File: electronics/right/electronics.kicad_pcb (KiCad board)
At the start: 2 copper layers, 109.6 x 73.9 mm, 90 parts, among them J3 USB_C_Receptacle_USB2.0, J4 Battery Connector, SW23 Choc v1 Socket, SW24 Choc v1 Socket, SW25 Choc v1 Socket, SW26 Choc v1 Socket, SW27 Choc v1 Socket, SW28 Choc v1 Socket, SW29 Choc v1 Socket, SW30 Choc v1 Socket, SW31 Choc v1 Socket, SW32 Choc v1 Socket, SW33 Choc v1 Socket, SW34 Choc v1 Socket, SW35 Choc v1 Socket, SW36 Choc v1 Socket, SW37 Choc v1 Socket, SW38 Choc v1 Socket, SW39 Choc v1 Socket, SW40 Choc v1 Socket, SW41 Choc v1 Socket, SW42 Choc v1 Socket, SW43 Choc v1 Socket, SW44 SW_Reset, U4 nRF52840, U5 ESDR0502NMUTAG, U6 BQ24075RGT, Y3 32.768 kHz, Y4 32MHz

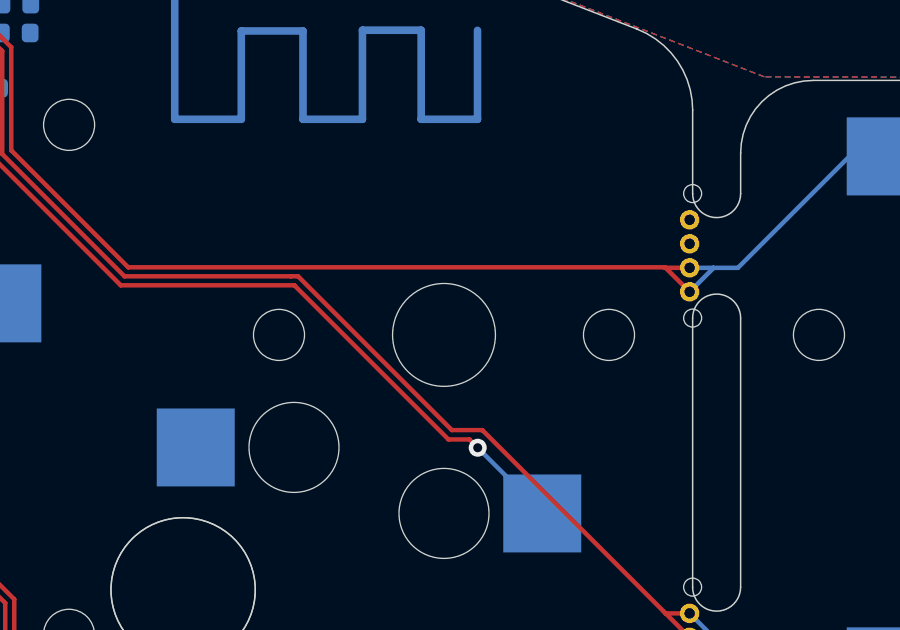
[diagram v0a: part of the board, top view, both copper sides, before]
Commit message: Extend ground plane fill.
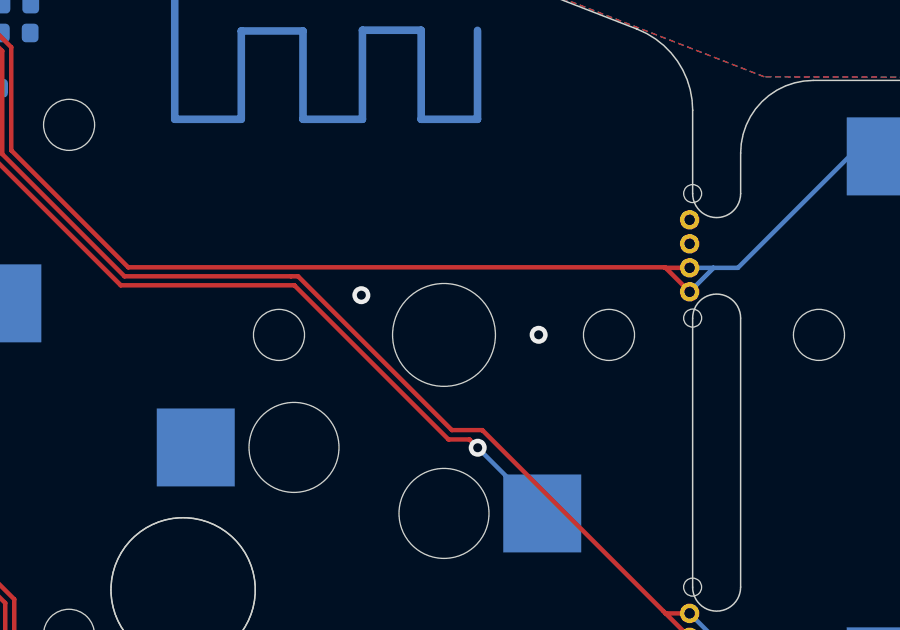
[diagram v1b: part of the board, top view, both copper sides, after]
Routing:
- net GND: vias 35 -> 37
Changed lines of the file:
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@@
   (via locked (at 82.38 33.089) (size 0.6) (drill 0.3) (layers "F.Cu" "B.Cu") (net 2))
   (via locked (at 86.94 29.25) (size 0.6) (drill 0.3) (layers "F.Cu" "B.Cu") (net 2))
+  (via (at 113.21 45.08) (size 0.6) (drill 0.3) (layers "F.Cu" "B.Cu") (free) (net 2))
   (via locked (at 104.84 32.239) (size 0.6) (drill 0.3) (layers "F.Cu" "B.Cu") (free) (net 2))
   (via locked (at 91.94 33.239) (size 0.6) (drill 0.3) (layers "F.Cu" "B.Cu") (free) (net 2))
@@
   (via locked (at 61.74 34.0995) (size 0.6) (drill 0.3) (layers "F.Cu" "B.Cu") (net 2))
   (via locked (at 81.58 33.089) (size 0.6) (drill 0.3) (layers "F.Cu" "B.Cu") (net 2))
+  (via (at 119.12 46.4) (size 0.6) (drill 0.3) (layers "F.Cu" "B.Cu") (free) (net 2))
   (via locked (at 95.54 30.839) (size 0.6) (drill 0.3) (layers "F.Cu" "B.Cu") (free) (net 2))
   (via locked (at 91.94 30.839) (size 0.6) (drill 0.3) (layers "F.Cu" "B.Cu") (free) (net 2))

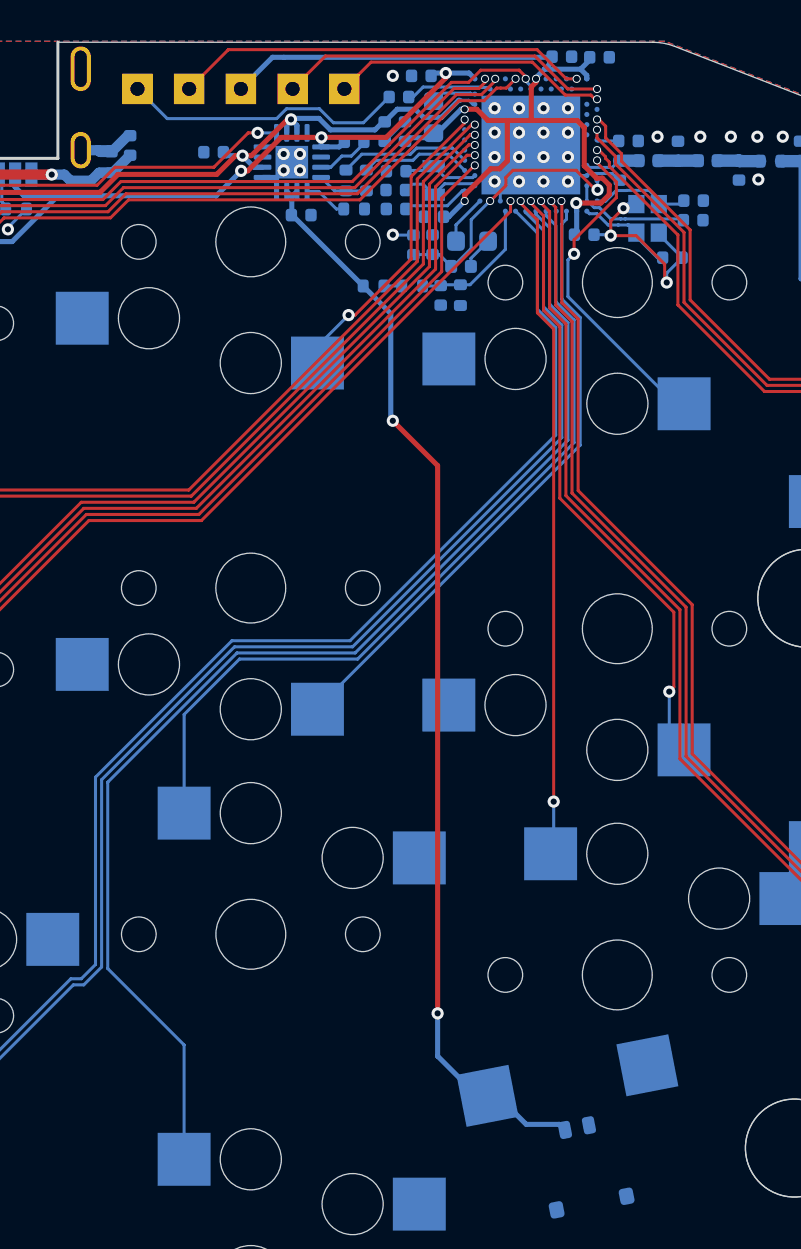
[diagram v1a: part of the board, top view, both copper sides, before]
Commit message: electronics/right: Fix schema and PCB references parity.
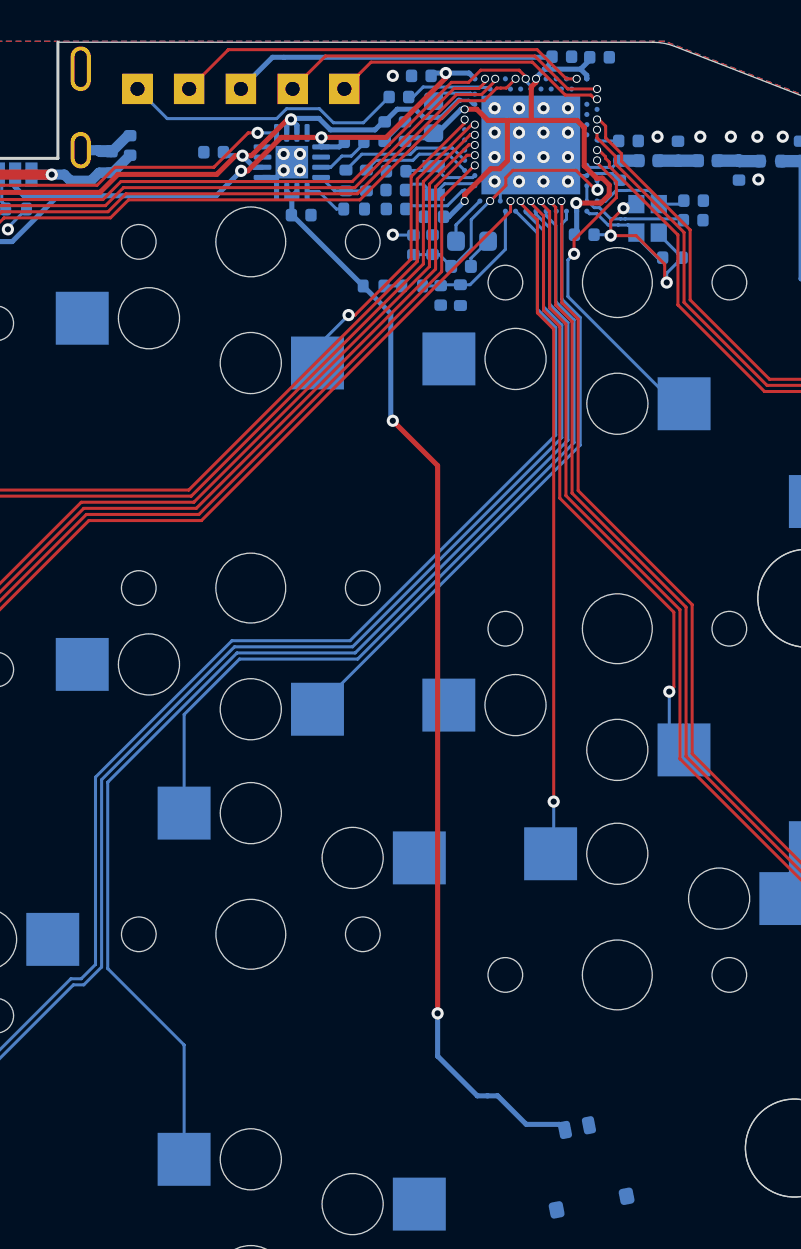
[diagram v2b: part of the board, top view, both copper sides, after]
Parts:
- removed ?: , 
- removed ?: , clipboard:cb50c767-9c7e-4e33-9f10-2a6feed7503c
- removed AE2: Antenna, lib:2.4GHz-meander-antenna-right
- removed C27, C31, C50: 1uF, lib:C_0402_1005Metric
- removed C28: 47nF, lib:C_0402_1005Metric
- removed C29, C30, C36, C37, C51, C52: 4.7uF, lib:C_0402_1005Metric
- removed C32, C33, C34, C40, C49: 100nF, lib:C_0402_1005Metric
- removed C35: 1nF, lib:C_0402_1005Metric
- removed C38: 100pF, lib:C_0402_1005Metric
- removed C39, C42, C47, C48: 15pF, lib:C_0402_1005Metric
- removed C41: 10nF, lib:C_0402_1005Metric
- removed C43: 1.5pF, lib:C_0402_1005Metric
- removed C44: N.C, lib:C_0402_1005Metric
- removed C45: 1.2pF, lib:C_0402_1005Metric
- removed C46: 1.0pF, lib:C_0402_1005Metric
- removed D3, D4: LED_Dual_KKA, lib:LED-ARRAY-SMD_3P-L3.0-W2.0-L-FD
- removed H5, H6, H7, H8: MountingHole, lib:screw-hole
- removed J3: USB_C_Receptacle_USB2.0, lib:USB-C-SMD_TYPE-C-31-M-13A-1
- removed J4: Battery Connector, lib:Molex_Pico-EZmate_78171-0002_1x02-1MP_P1.20mm_Vertical
- removed L10: 4.7nH, Inductor_SMD:L_0402_1005Metric
- removed L6: 15nH, Inductor_SMD:L_0402_1005Metric
- removed L7, L8: 10uH, Inductor_SMD:L_0603_1608Metric
- removed L9: 2.2nH, Inductor_SMD:L_0402_1005Metric
- removed NT2: NetTie_2, lib:net-tie-2-tiny
- removed R13: 10M, lib:R_0402_1005Metric
- removed R14, R15: 2M, lib:R_0402_1005Metric
- removed R16: 0R, lib:R_0402_1005Metric
- removed R17: 1.5k, lib:R_0402_1005Metric
- removed R18: 1M, lib:R_0402_1005Metric
- removed R19, R20: 5.1k, lib:R_0402_1005Metric
- removed R21, R22, R23: 10k, lib:R_0402_1005Metric
- removed R24: 3.9k, lib:R_0402_1005Metric
- removed SW23, SW24, SW25, SW26, SW27, SW28, SW29, SW30, SW31, SW32, SW33, SW34, SW35, SW36, SW37, SW38, SW39, SW40, SW41, SW42, SW43: Choc v1 Socket, lib:Kailh_socket_PG1350
- removed SW44: SW_Reset, lib:Panasonic_EVQPUL_EVQPUC
- removed TP10: GND, TestPoint:TestPoint_THTPad_1.5x1.5mm_Drill0.7mm
- removed TP6: SWO, TestPoint:TestPoint_THTPad_1.5x1.5mm_Drill0.7mm
- removed TP7: SWC, TestPoint:TestPoint_THTPad_1.5x1.5mm_Drill0.7mm
- removed TP8: SWD, TestPoint:TestPoint_THTPad_1.5x1.5mm_Drill0.7mm
- removed TP9: 3.3V, TestPoint:TestPoint_THTPad_1.5x1.5mm_Drill0.7mm
- removed U4: nRF52840, Package_DFN_QFN:Nordic_AQFN-73-1EP_7x7mm_P0.5mm
- removed U5: ESDR0502NMUTAG, lib:ESDR0502NMUTAG
- removed U6: BQ24075RGT, lib:VQFN-16-1EP_3x3mm_P0.5mm_EP1.6x1.6mm
- removed Y3: 32.768 kHz, lib:Crystal_SMD_2012-2Pin_2.0x1.2mm
- removed Y4: 32MHz, lib:Crystal_SMD_2016-4Pin_2.0x1.6mm
- added AE1: Antenna, lib:2.4GHz-meander-antenna-right, F.Cu at (107.0, 33.5)
- added C1: 1uF, Capacitor_SMD:C_0402_1005Metric, B.Cu at (88.9, 37.5)
- added C10: 4.7uF, Capacitor_SMD:C_0402_1005Metric, B.Cu at (88.3, 29.3)
- added C11: 4.7uF, Capacitor_SMD:C_0402_1005Metric, B.Cu at (87.2, 30.3)
- added C12: 100pF, Capacitor_SMD:C_0402_1005Metric, B.Cu at (101.7, 36.3)
- added C13: 15pF, Capacitor_SMD:C_0402_1005Metric, B.Cu at (87.1, 34.9)
- added C14: 100nF, Capacitor_SMD:C_0402_1005Metric, B.Cu at (87.1, 35.8)
- added C15: 10nF, Capacitor_SMD:C_0402_1005Metric, B.Cu at (89.3, 40.0)
- added C16: 15pF, Capacitor_SMD:C_0402_1005Metric, B.Cu at (87.1, 33.9)
- added C17: 1.5pF, Capacitor_SMD:C_0402_1005Metric, B.Cu at (106.9, 32.9)
- added C18: N.C, Capacitor_SMD:C_0402_1005Metric, B.Cu at (103.9, 33.9)
- added C19: 1.2pF, Capacitor_SMD:C_0402_1005Metric, B.Cu at (100.9, 32.9)
- added C2: 47nF, Capacitor_SMD:C_0402_1005Metric, B.Cu at (88.0, 37.5)
- added C20: 1.0pF, Capacitor_SMD:C_0402_1005Metric, B.Cu at (98.1, 33.9)
- added C21: 15pF, Capacitor_SMD:C_0402_1005Metric, B.Cu at (101.7, 35.4)
- added C22: 15pF, Capacitor_SMD:C_0402_1005Metric, B.Cu at (100.7, 38.2)
- added C23: 100nF, Capacitor_SMD:C_0402_1005Metric, B.Cu at (74.0, 32.7)
- added C24: 1uF, Capacitor_SMD:C_0402_1005Metric, B.Cu at (85.0, 32.5)
- added C25: 4.7uF, Capacitor_SMD:C_0402_1005Metric, B.Cu at (86.5, 32.0)
- added C26: 4.7uF, Capacitor_SMD:C_0402_1005Metric, B.Cu at (82.4, 36.1)
- added C3: 4.7uF, Capacitor_SMD:C_0402_1005Metric, B.Cu at (78.1, 33.0)
- added C4: 4.7uF, Capacitor_SMD:C_0402_1005Metric, B.Cu at (87.5, 32.0)
- added C5: 1uF, Capacitor_SMD:C_0402_1005Metric, B.Cu at (96.3, 37.0)
- added C6: 100nF, Capacitor_SMD:C_0402_1005Metric, B.Cu at (95.2, 28.3)
- added C7: 100nF, Capacitor_SMD:C_0402_1005Metric, B.Cu at (97.1, 28.3)
- added C8: 100nF, Capacitor_SMD:C_0402_1005Metric, B.Cu at (89.0, 36.2)
- added C9: 1nF, Capacitor_SMD:C_0402_1005Metric, B.Cu at (98.5, 32.4)
- added D1: LED_Dual_KKA, lib:LED-ARRAY-SMD_3P-L3.0-W2.0-L-FD, B.Cu at (41.8, 34.3)
- added D2: LED_Dual_KKA, lib:LED-ARRAY-SMD_3P-L3.0-W2.0-L-FD, B.Cu at (54.3, 30.5)
- added H1: MountingHole, lib:screw-hole, F.Cu at (52.7, 52.9)
- added H2: MountingHole, lib:screw-hole, F.Cu at (107.3, 54.9)
- added H3: MountingHole, lib:screw-hole, F.Cu at (53.3, 83.9)
- added H4: MountingHole, lib:screw-hole, B.Cu at (106.7, 81.9)
- added J1: USB_C_Receptacle_USB2.0, lib:USB-C-SMD_TYPE-C-31-M-13A-1, B.Cu at (66.0, 31.5)
- added J2: Molex_781710002, lib:Molex_Pico-EZmate_78171-0002_1x02-1MP_P1.20mm_Vertical, B.Cu at (96.3, 82.7)
- added L1: 15nH, Inductor_SMD:L_0402_1005Metric, B.Cu at (90.3, 38.6)
- added L2: 10uH, Inductor_SMD:L_0603_1608Metric, B.Cu at (90.8, 37.4)
- added L3: 10uH, Inductor_SMD:L_0603_1608Metric, B.Cu at (88.9, 31.3)
- added L4: 2.2nH, Inductor_SMD:L_0402_1005Metric, B.Cu at (102.4, 33.4)
- added L5: 4.7nH, Inductor_SMD:L_0402_1005Metric, B.Cu at (99.5, 33.4)
- added NT1: NetTie_2, lib:net-tie-2-tiny, B.Cu at (96.2, 34.1)
- added R1: 10M, Resistor_SMD:R_0402_1005Metric, B.Cu at (90.3, 40.0)
- added R10: 10k, Resistor_SMD:R_0402_1005Metric, B.Cu at (85.6, 34.4)
- added R11: 10k, Resistor_SMD:R_0402_1005Metric, B.Cu at (53.3, 33.2)
- added R12: 3.9k, Resistor_SMD:R_0402_1005Metric, B.Cu at (84.6, 34.4)
- added R2: 2M, Resistor_SMD:R_0402_1005Metric, B.Cu at (87.9, 39.6)
- added R3: 2M, Resistor_SMD:R_0402_1005Metric, B.Cu at (86.0, 39.6)
- added R4: 0R, Resistor_SMD:R_0402_1005Metric, B.Cu at (105.5, 33.4)
- added R5: 1.5k, Resistor_SMD:R_0402_1005Metric, B.Cu at (41.2, 36.3)
- added R6: 1M, Resistor_SMD:R_0402_1005Metric, B.Cu at (73.1, 33.5)
- added R7: 5.1k, Resistor_SMD:R_0402_1005Metric, B.Cu at (68.4, 35.8)
- added R8: 5.1k, Resistor_SMD:R_0402_1005Metric, B.Cu at (64.2, 36.0)
- added R9: 10k, Resistor_SMD:R_0402_1005Metric, B.Cu at (85.0, 35.8)
- added SW1: CPG135001S30, lib:Kailh_socket_PG1350, B.Cu at (44.0, 44.4)
- added SW10: CPG135001S30, lib:Kailh_socket_PG1350, B.Cu at (98.0, 56.4)
- added SW11: CPG135001S30, lib:Kailh_socket_PG1350, B.Cu at (116.0, 63.4)
- added SW12: CPG135001S30, lib:Kailh_socket_PG1350, B.Cu at (134.0, 63.4)
- added SW13: CPG135001S30, lib:Kailh_socket_PG1350, B.Cu at (44.0, 78.4)
- added SW14: CPG135001S30, lib:Kailh_socket_PG1350, B.Cu at (62.0, 75.4)
- added SW15: CPG135001S30, lib:Kailh_socket_PG1350, B.Cu at (80.0, 71.4)
- added SW16: CPG135001S30, lib:Kailh_socket_PG1350, B.Cu at (98.0, 73.4)
- added SW17: CPG135001S30, lib:Kailh_socket_PG1350, B.Cu at (116.0, 80.4)
- added SW18: CPG135001S30, lib:Kailh_socket_PG1350, B.Cu at (134.0, 80.4)
- added SW19: CPG135001S30, lib:Kailh_socket_PG1350, B.Cu at (44.0, 95.4)
- added SW2: CPG135001S30, lib:Kailh_socket_PG1350, B.Cu at (62.0, 41.4)
- added SW20: CPG135001S30, lib:Kailh_socket_PG1350, B.Cu at (62.0, 92.4)
- added SW21: CPG135001S30, lib:Kailh_socket_PG1350, B.Cu at (80.0, 88.4)
- added SW22: EVQPUC02K, lib:Panasonic_EVQPUL_EVQPUC, B.Cu at (48.3, 33.2)
- added SW3: CPG135001S30, lib:Kailh_socket_PG1350, B.Cu at (80.0, 37.4)
- added SW4: CPG135001S30, lib:Kailh_socket_PG1350, B.Cu at (98.0, 39.4)
- added SW5: CPG135001S30, lib:Kailh_socket_PG1350, B.Cu at (116.0, 46.4)
- added SW6: CPG135001S30, lib:Kailh_socket_PG1350, B.Cu at (134.0, 46.4)
- added SW7: CPG135001S30, lib:Kailh_socket_PG1350, B.Cu at (44.0, 61.4)
- added SW8: CPG135001S30, lib:Kailh_socket_PG1350, B.Cu at (62.0, 58.4)
- added SW9: CPG135001S30, lib:Kailh_socket_PG1350, B.Cu at (80.0, 54.4)
- added TP1: SWO, TestPoint:TestPoint_THTPad_1.5x1.5mm_Drill0.7mm, B.Cu at (76.9, 29.9)
- added TP2: SWC, TestPoint:TestPoint_THTPad_1.5x1.5mm_Drill0.7mm, B.Cu at (84.6, 29.9)
- added TP3: SWD, TestPoint:TestPoint_THTPad_1.5x1.5mm_Drill0.7mm, B.Cu at (82.0, 29.9)
- added TP4: 3.3V, TestPoint:TestPoint_THTPad_1.5x1.5mm_Drill0.7mm, B.Cu at (79.5, 29.9)
- added TP5: GND, TestPoint:TestPoint_THTPad_1.5x1.5mm_Drill0.7mm, B.Cu at (74.4, 29.9)
- added U1: nRF52840, Package_DFN_QFN:Nordic_AQFN-73-1EP_7x7mm_P0.5mm, B.Cu at (93.7, 32.6)
- added U2: ESDR0502NMUTAG, lib:ESDR0502NMUTAG, B.Cu at (65.5, 37.0)
- added U3: BQ24075RGT, Package_DFN_QFN:VQFN-16-1EP_3x3mm_P0.5mm_EP1.6x1.6mm, B.Cu at (82.0, 33.5)
- added Y1: 32.768 kHz, lib:Crystal_SMD_2012-2Pin_2.0x1.2mm, B.Cu at (88.9, 34.4)
- added Y2: 32MHz, lib:Crystal_SMD_2016-4Pin_2.0x1.6mm, B.Cu at (99.5, 36.2)
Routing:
- net Net-(U4-P0.15): track 55.2 -> 0.00 mm, vias 2 -> 0
- net Net-(U1-P0.15): track 0.00 -> 55.2 mm, vias 0 -> 2
- net Net-(U4-D+): track 35.0 -> 0.00 mm, vias 3 -> 0
- net Net-(U1-D+): track 0.00 -> 35.0 mm, vias 0 -> 3
- net Net-(U4-D-): track 32.7 -> 0.00 mm, vias 3 -> 0
- net Net-(U1-D-): track 0.00 -> 32.7 mm, vias 0 -> 3
- net Net-(D4-K2): track 29.5 -> 0.00 mm, vias 2 -> 0
- net Net-(D2-K2): track 0.00 -> 29.5 mm, vias 0 -> 2
- net Net-(U4-TRACEDATA0/P1.00): track 20.3 -> 0.00 mm, vias 1 -> 0
- net Net-(U1-TRACEDATA0/P1.00): track 0.00 -> 20.3 mm, vias 0 -> 1
- net Net-(U4-SWDIO): track 16.1 -> 0.00 mm, vias 1 -> 0
- net Net-(U1-SWDIO): track 0.00 -> 16.1 mm, vias 0 -> 1
- net Net-(U4-SWDCLK): track 13.7 -> 0.00 mm, vias 1 -> 0
- net Net-(U1-SWDCLK): track 0.00 -> 13.7 mm, vias 0 -> 1
- net Net-(U4-DEC4): track 13.0 -> 0.00 mm, vias 2 -> 0
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
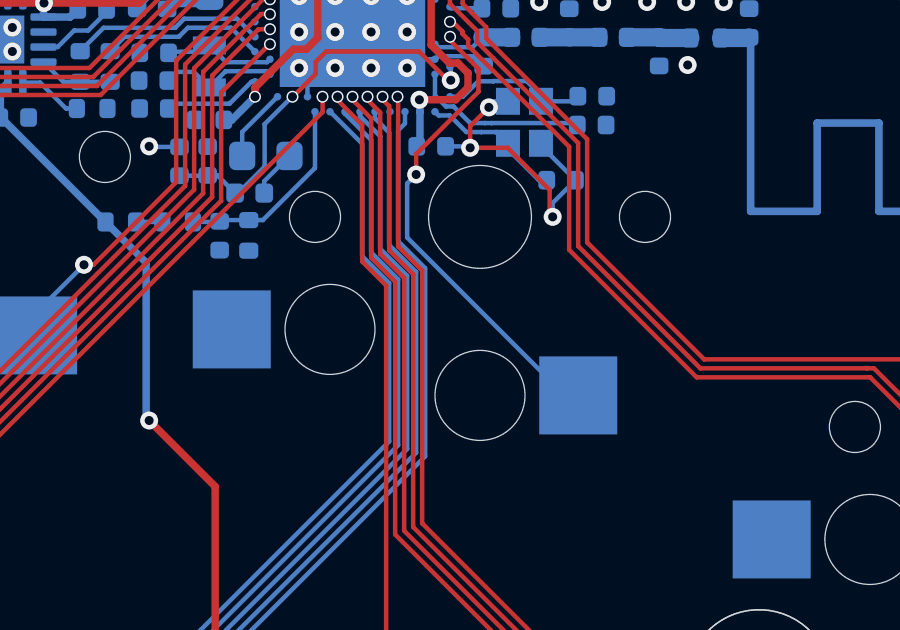
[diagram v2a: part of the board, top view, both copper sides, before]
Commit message: Remove footprint placement silkscreen lines.
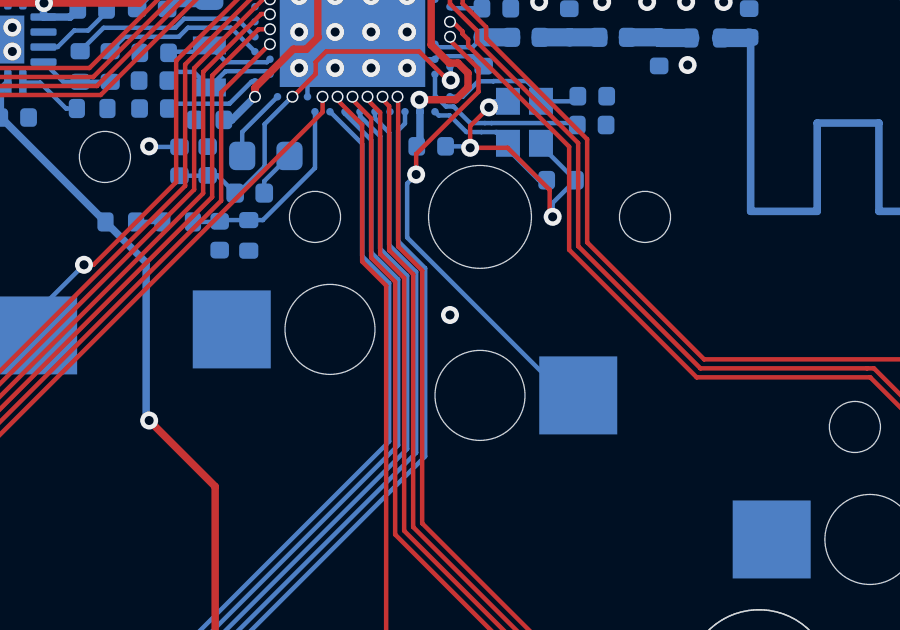
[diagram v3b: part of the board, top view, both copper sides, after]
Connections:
- mouse-bite-5mm-slot pad : K6 -> GND
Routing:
- net GND: vias 37 -> 38
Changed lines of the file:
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@@
     (pad "" thru_hole circle locked (at 1.675 -0.1 90) (size 0.65 0.65) (drill 0.35) (layers "*.Cu" "*.Mask")
       (net 15 "K6"))
-    (pad "" thru_hole circle locked (at 2.475 -0.1 90) (size 0.65 0.65) (drill 0.35) (layers "*.Cu" "*.Mask"))
-    (pad "" thru_hole circle locked (at 3.275 -0.1 90) (size 0.65 0.65) (drill 0.35) (layers "*.Cu" "*.Mask"))
+    (pad "" thru_hole circle locked (at 2.475 -0.1 90) (size 0.65 0.65) (drill 0.35) (layers "*.Cu" "*.Mask")
+      (net 2 "GND"))
+    (pad "" thru_hole circle locked (at 3.275 -0.1 90) (size 0.65 0.65) (drill 0.35) (layers "*.Cu" "*.Mask")
+      (net 2 "GND"))
     (pad "" np_thru_hole circle locked (at 4.15 0 90) (size 0.6 0.6) (drill 0.6) (layers "F&B.Cu" "*.Mask"))
   )
@@
   (via locked (at 94.34 33.239) (size 0.6) (drill 0.3) (layers "F.Cu" "B.Cu") (free) (net 2))
   (via locked (at 94.34 34.439) (size 0.6) (drill 0.3) (layers "F.Cu" "B.Cu") (free) (net 2))
+  (via (at 96.968 42.672) (size 0.6) (drill 0.3) (layers "F.Cu" "B.Cu") (free) (net 2))
   (via locked (at 99.94 32.239) (size 0.6) (drill 0.3) (layers "F.Cu" "B.Cu") (free) (net 2))
   (via locked (at 94.34 32.039) (size 0.6) (drill 0.3) (layers "F.Cu" "B.Cu") (free) (net 2))

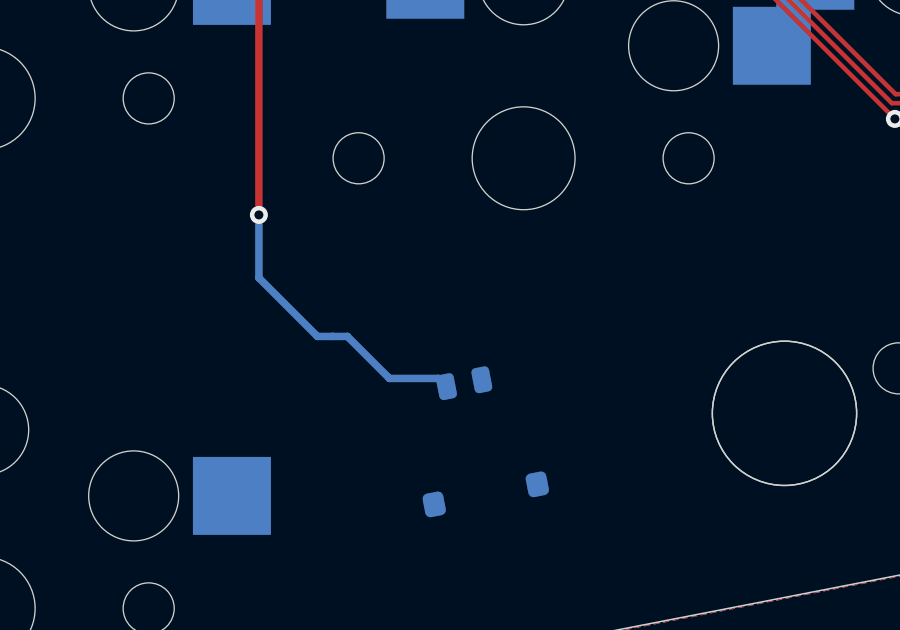
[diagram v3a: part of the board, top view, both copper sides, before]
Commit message: electronics/right: Add missing battery pads.
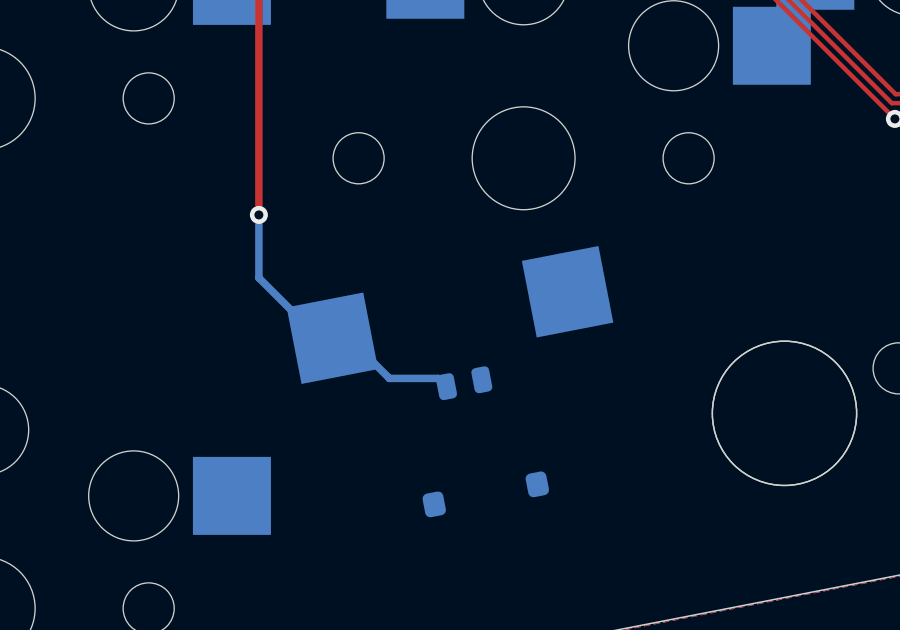
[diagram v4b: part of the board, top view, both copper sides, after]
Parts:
- added ?: , , F.Cu at (99.4, 77.9)
- added ?: , , F.Cu at (91.6, 79.4)

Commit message: Make sure left and right halves produce the same BOM.
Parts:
- C10: value 4.7uF -> 100nF
- C15: value 10nF -> 15pF
- C16: value 15pF -> 10nF
- C4: value 4.7uF -> 1nF
- C5: value 1uF -> 4.7uF
- C6: value 100nF -> 4.7uF
- C7: value 100nF -> 1uF
- C9: value 1nF -> 100nF
- R1: value 10M -> 2M
- R3: value 2M -> 10M
- moved C5 11.2 mm to (88.3, 29.3)
- moved C4 11.0 mm to (98.5, 32.4), turned to 0 degrees
- moved C15 6.48 mm to (87.1, 33.9), turned to 0 degrees
- moved C16 6.48 mm to (89.3, 40.0), turned to 90 degrees
- moved C9 5.09 mm to (96.3, 37.0), turned to 180 degrees
- moved R1 4.29 mm to (86.0, 39.6), turned to 0 degrees
- moved R3 4.29 mm to (90.3, 40.0), turned to -90 degrees
- moved C10 2.85 mm to (87.5, 32.0), turned to -90 degrees
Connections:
- C10 pad 1: VBUS -> GND
- C10 pad 2: GND -> V_DD
- C15 pad 2: BAT_VOLT -> Net-(U1-XL2/P0.01)
- C16 pad 2: Net-(U1-XL2/P0.01) -> BAT_VOLT
- C4 pad 1: GND -> Net-(U1-DEC5)
- C4 pad 2: V_DD -> GND
- C5 pad 1: GND -> VBUS
- C5 pad 2: V_DD -> GND
- C9 pad 1: Net-(U1-DEC5) -> GND
- C9 pad 2: GND -> V_DD
- R1 pad 1: BAT_VOLT -> VBAT
- R1 pad 2: GND -> Net-(R1-Pad2)
- R2 pad 1: Net-(R2-Pad1) -> Net-(R1-Pad2)
- R3 pad 1: VBAT -> BAT_VOLT
- R3 pad 2: Net-(R2-Pad1) -> GND
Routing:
- net Net-(R2-Pad1): track 0.88 -> 0.00 mm
- net Net-(R1-Pad2): track 0.00 -> 0.88 mm
